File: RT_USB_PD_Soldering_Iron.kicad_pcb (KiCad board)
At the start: 4 copper layers, 75 x 11 mm, 64 parts, among them J1 USB4105-GF-A, J2 35RASMT4BHNTRX, J3 Conn_02x03_Odd_Even, SW1 SW_Push, SW2 SW_Push, U1 SPX3819M5-L-3-3, U2 ECMF02-AMX6, U3 FUSB302BMPX, U4 STM32G431Kxxx, U5 TPS25982ONRGET, U6 BMI270, U7 OPA376AIDCKR

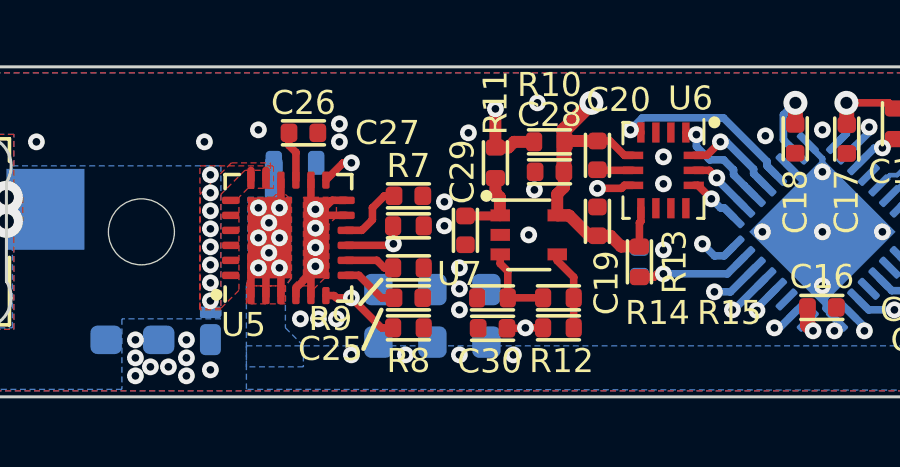
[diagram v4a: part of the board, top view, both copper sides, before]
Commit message: Update VQFN24 Footprint
update the footprint for slightly elongated pads.
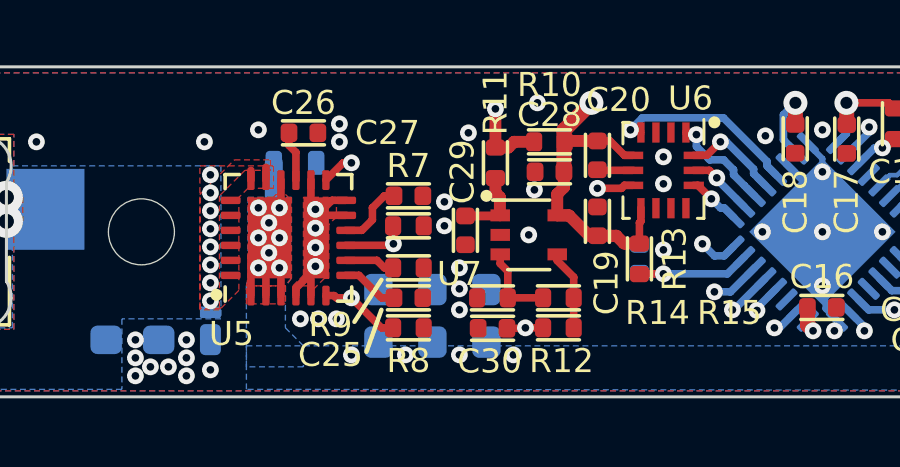
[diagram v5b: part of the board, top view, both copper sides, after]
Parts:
- moved C31 0.10 mm to (136.1, 125.9)
- moved R13 0.10 mm to (136.1, 125.9)
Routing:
- net /BOARD_TEMP: track 34.3 -> 35.1 mm

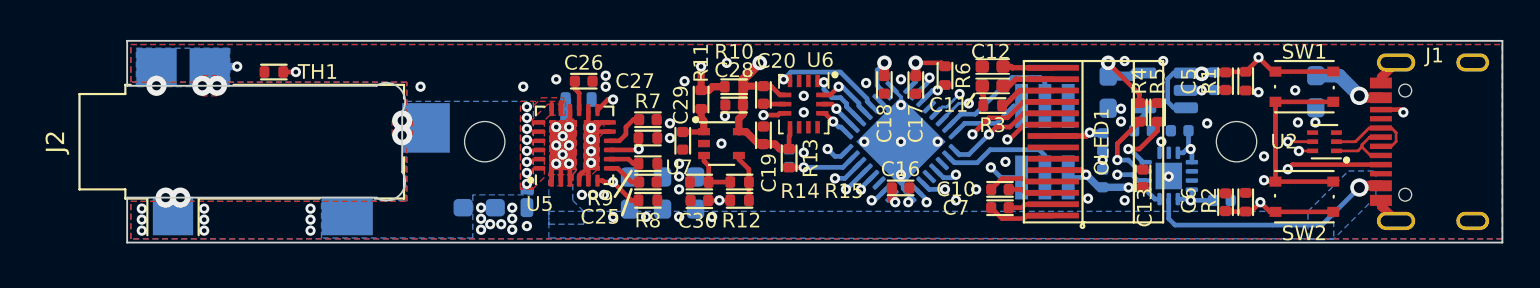
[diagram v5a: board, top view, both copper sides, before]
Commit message: Housekeeping
cleanup. Moved R6. Update USB4105 connector (elongate holes slightly)
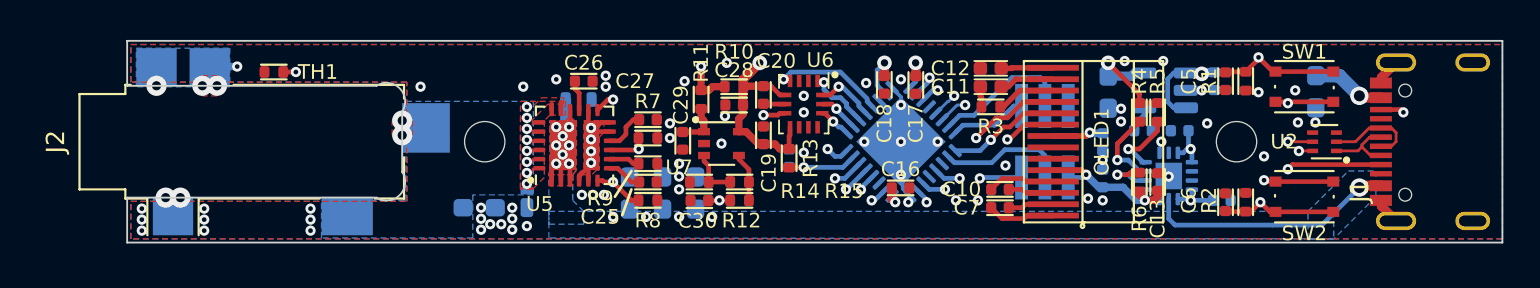
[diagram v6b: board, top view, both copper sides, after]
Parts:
- moved R6 12.1 mm to (155.2, 127.2), turned to 90 degrees
- moved C13 0.82 mm to (156.2, 127.2)
- moved C12 0.14 mm to (147.1, 121.0)
- moved R3 0.12 mm to (147.1, 123.1)
- moved C11 0.11 mm to (147.1, 122.0)
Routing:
- net /FUSB_INT_N: track 15.8 -> 16.6 mm
- net +3V3: track 88.6 -> 88.4 mm, vias 9 -> 10

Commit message: Update OLED keepout, 3D models
increase the keepout slightly.
add more 3D models
fix error in USB4105 layout
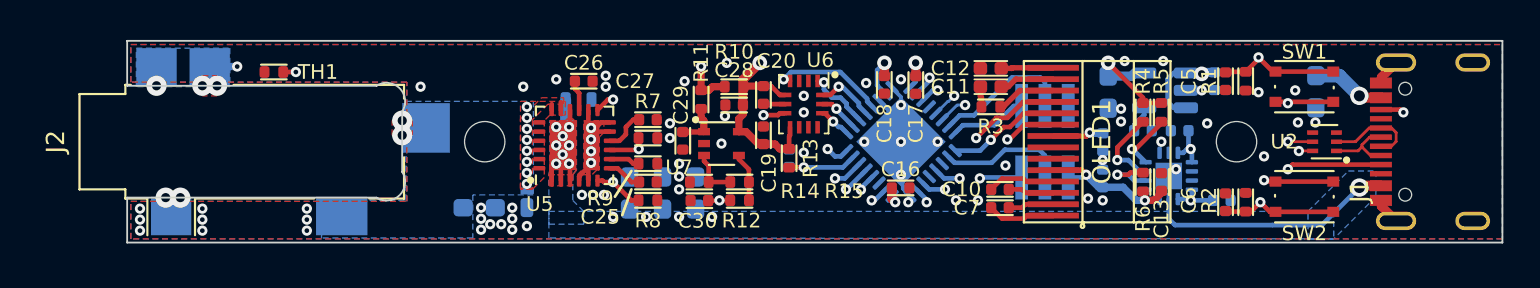
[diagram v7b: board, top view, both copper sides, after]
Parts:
- SW1, SW2: footprint local:SW_Push_1P1T_NO_Vertical_Wuerth_434133025816 -> local:SW_Push_1P1T_NO_Vertical_Wuerth_435171014816
- moved C13 0.20 mm to (156.4, 127.2)
- moved R4 0.20 mm to (155.4, 123.4)
- moved R6 0.20 mm to (155.4, 127.2)
- moved R5 0.20 mm to (156.4, 123.4)

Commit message: Change mounting holes to Plated Through Holes
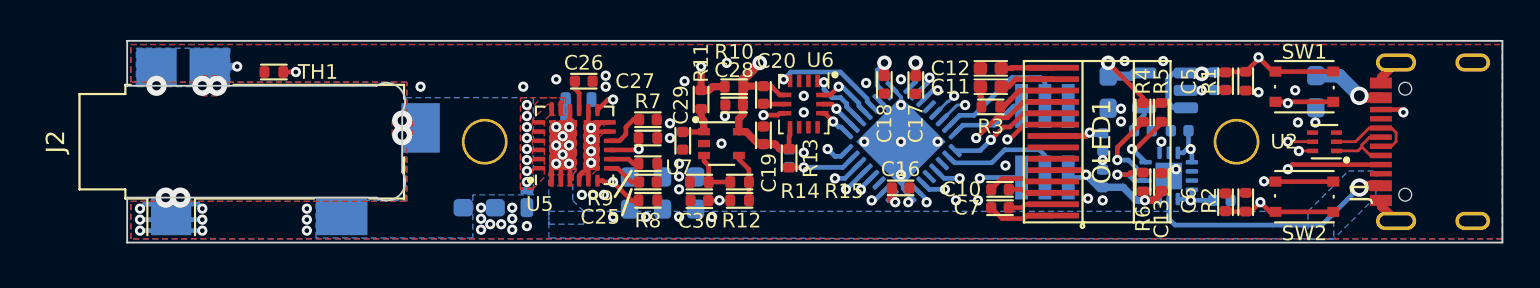
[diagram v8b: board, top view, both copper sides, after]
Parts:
- H1, H2: footprint MountingHole:MountingHole_2.2mm_M2_ISO7380 -> local:MountingHole_2.2mm_M2_ISO7380_Pad
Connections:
- H1 pad 1: (no net) -> GND
- H2 pad 1: (no net) -> GND
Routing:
- net GND: track 17.0 -> 28.8 mm, vias 72 -> 70
